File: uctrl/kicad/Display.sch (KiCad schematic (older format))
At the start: 34 parts, among them P201 CONN_01X06, P202 CONN_01X07, P203 CONN_01X06, P204 CONN_01X07, Q201 BC856BS, Q202 BC856BS, Q203 BC856BS, U201 SN74LS138, U202 74HC4511

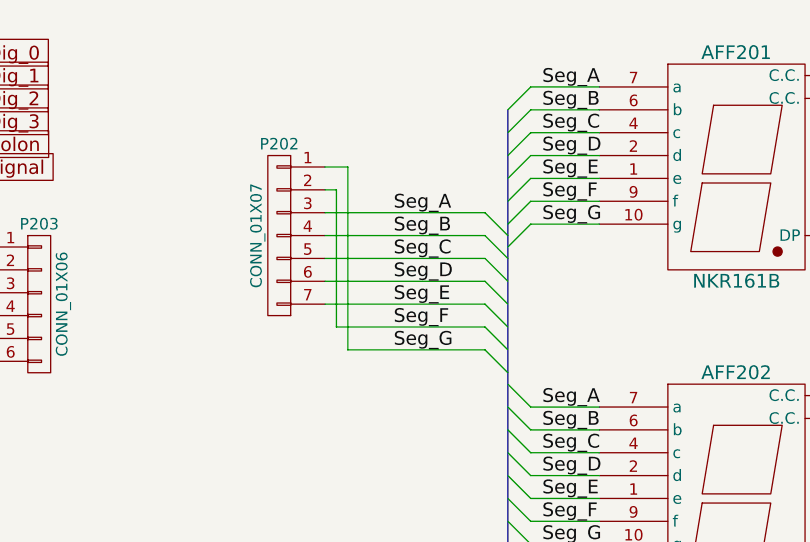
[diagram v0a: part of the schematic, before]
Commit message: Correction to segments F and G!
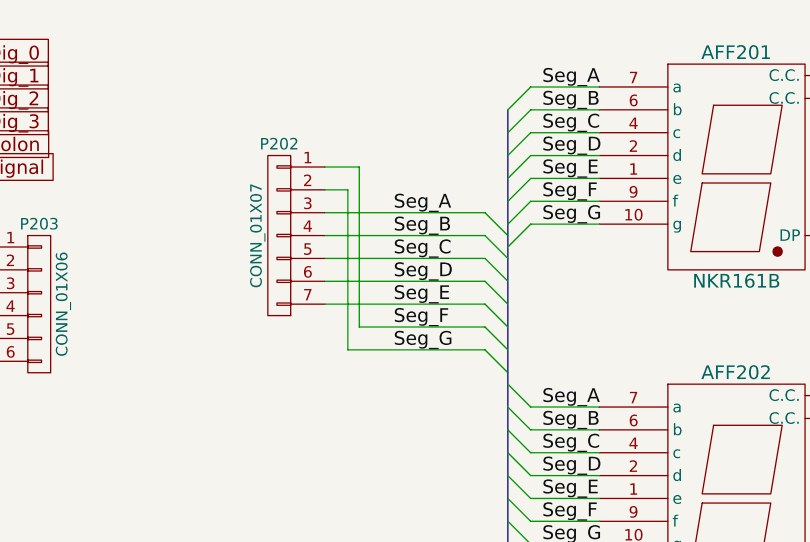
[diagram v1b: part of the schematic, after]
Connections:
- net Seg_F: now also P202.1 (P1); no longer P202.2 (P2)
- net Seg_G: now also P202.2 (P2); no longer P202.1 (P1)
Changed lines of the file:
@@
 	7050 1850 7750 1850
 Wire Wire Line
-	7100 1950 7750 1950
+	7200 1950 7750 1950
 Wire Wire Line
 	7150 2050 7750 2050
@@
 	5200 5650 5350 5650
 Wire Wire Line
-	7100 1950 7100 1350
-Wire Wire Line
-	7100 1350 7050 1350
-Wire Wire Line
-	7150 2050 7150 1250
-Wire Wire Line
-	7150 1250 7050 1250
+	7200 1250 7200 1950
+Wire Wire Line
+	7150 2050 7150 1350
+Wire Wire Line
+	7150 1350 7050 1350
+Wire Wire Line
+	7200 1250 7050 1250
 $EndSCHEMATC

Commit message: Updated the seven segment foot print and added the mounting tabs
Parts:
- AFF201, AFF202, AFF203, AFF204: footprint ClockFootprints:161_163_Series -> ClockFootprints:161_163_Series_extended
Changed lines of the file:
@@
 F 0 "AFF201" H 8850 1850 60  0000 C CNN
 F 1 "NKR161B" H 8850 850 60  0000 C CNN
-F 2 "ClockFootprints:161_163_Series" H 8850 1300 60  0001 C CNN
+F 2 "ClockFootprints:161_163_Series_extended" H 8850 1300 60  0001 C CNN
 F 3 "" H 8850 1300 60  0000 C CNN
 F 4 "NKR161B" H 8850 1300 60  0001 C CNN "MPN"
@@
 F 0 "AFF202" H 8850 3250 60  0000 C CNN
 F 1 "NKR161B" H 8850 2250 60  0000 C CNN
-F 2 "ClockFootprints:161_163_Series" H 8850 2700 60  0001 C CNN
+F 2 "ClockFootprints:161_163_Series_extended" H 8850 2700 60  0001 C CNN
 F 3 "" H 8850 2700 60  0000 C CNN
 F 4 "NKR161B" H 8850 2700 60  0001 C CNN "MPN"
@@
 F 0 "AFF203" H 8850 4750 60  0000 C CNN
 F 1 "NKR161B" H 8850 3750 60  0000 C CNN
-F 2 "ClockFootprints:161_163_Series" H 8850 4200 60  0001 C CNN
+F 2 "ClockFootprints:161_163_Series_extended" H 8850 4200 60  0001 C CNN
 F 3 "" H 8850 4200 60  0000 C CNN
 F 4 "NKR161B" H 8850 4200 60  0001 C CNN "MPN"
@@
 F 0 "AFF204" H 8850 6050 60  0000 C CNN
 F 1 "NKR161B" H 8850 5050 60  0000 C CNN
-F 2 "ClockFootprints:161_163_Series" H 8850 5500 60  0001 C CNN
+F 2 "ClockFootprints:161_163_Series_extended" H 8850 5500 60  0001 C CNN
 F 3 "" H 8850 5500 60  0000 C CNN
 F 4 "NKR161B" H 8850 5500 60  0001 C CNN "MPN"
